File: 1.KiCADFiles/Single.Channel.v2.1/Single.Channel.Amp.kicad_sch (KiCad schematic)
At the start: 18 parts, among them J2 Conn_01x08, J3 Conn_01x04, J4 Conn_Coaxial_In, J5 Conn_Coaxial_Out, Q1 MMBT3904, Q2 MMBT3906

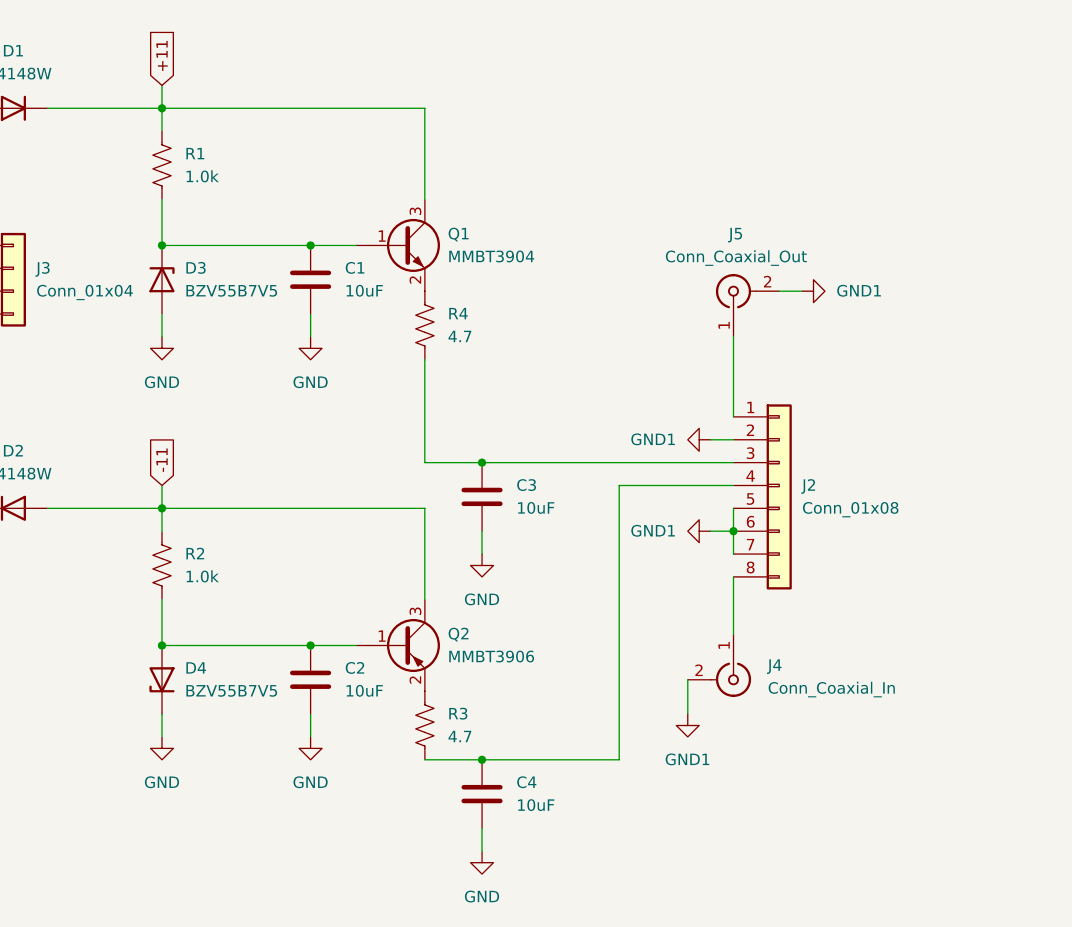
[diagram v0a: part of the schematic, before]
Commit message: Updated schematic with new Zener Component, updated componenet list
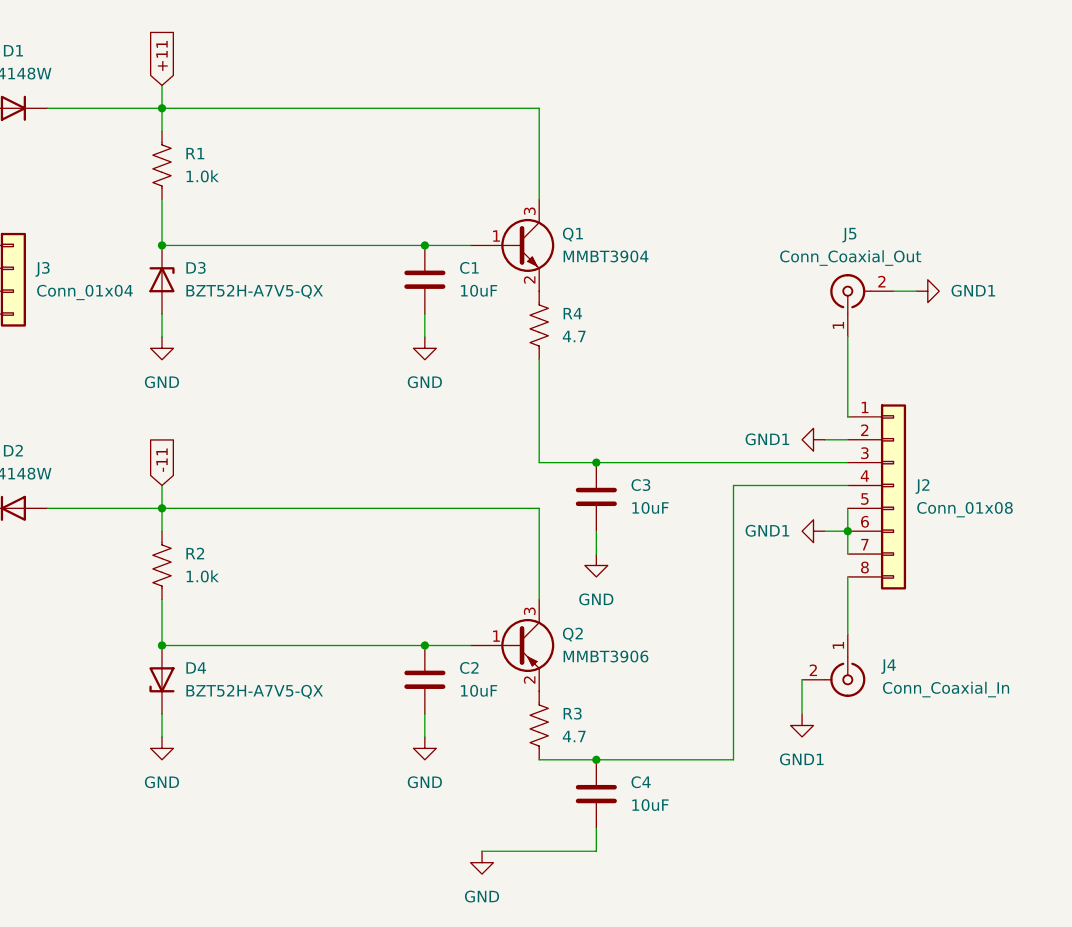
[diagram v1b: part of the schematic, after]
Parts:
- D3, D4: value BZV55B7V5 -> BZT52H-A7V5-QX
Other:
- moved on the sheet: C1, C2, C3, C4, J2, J4, J5, Q1, Q2, R3, R4

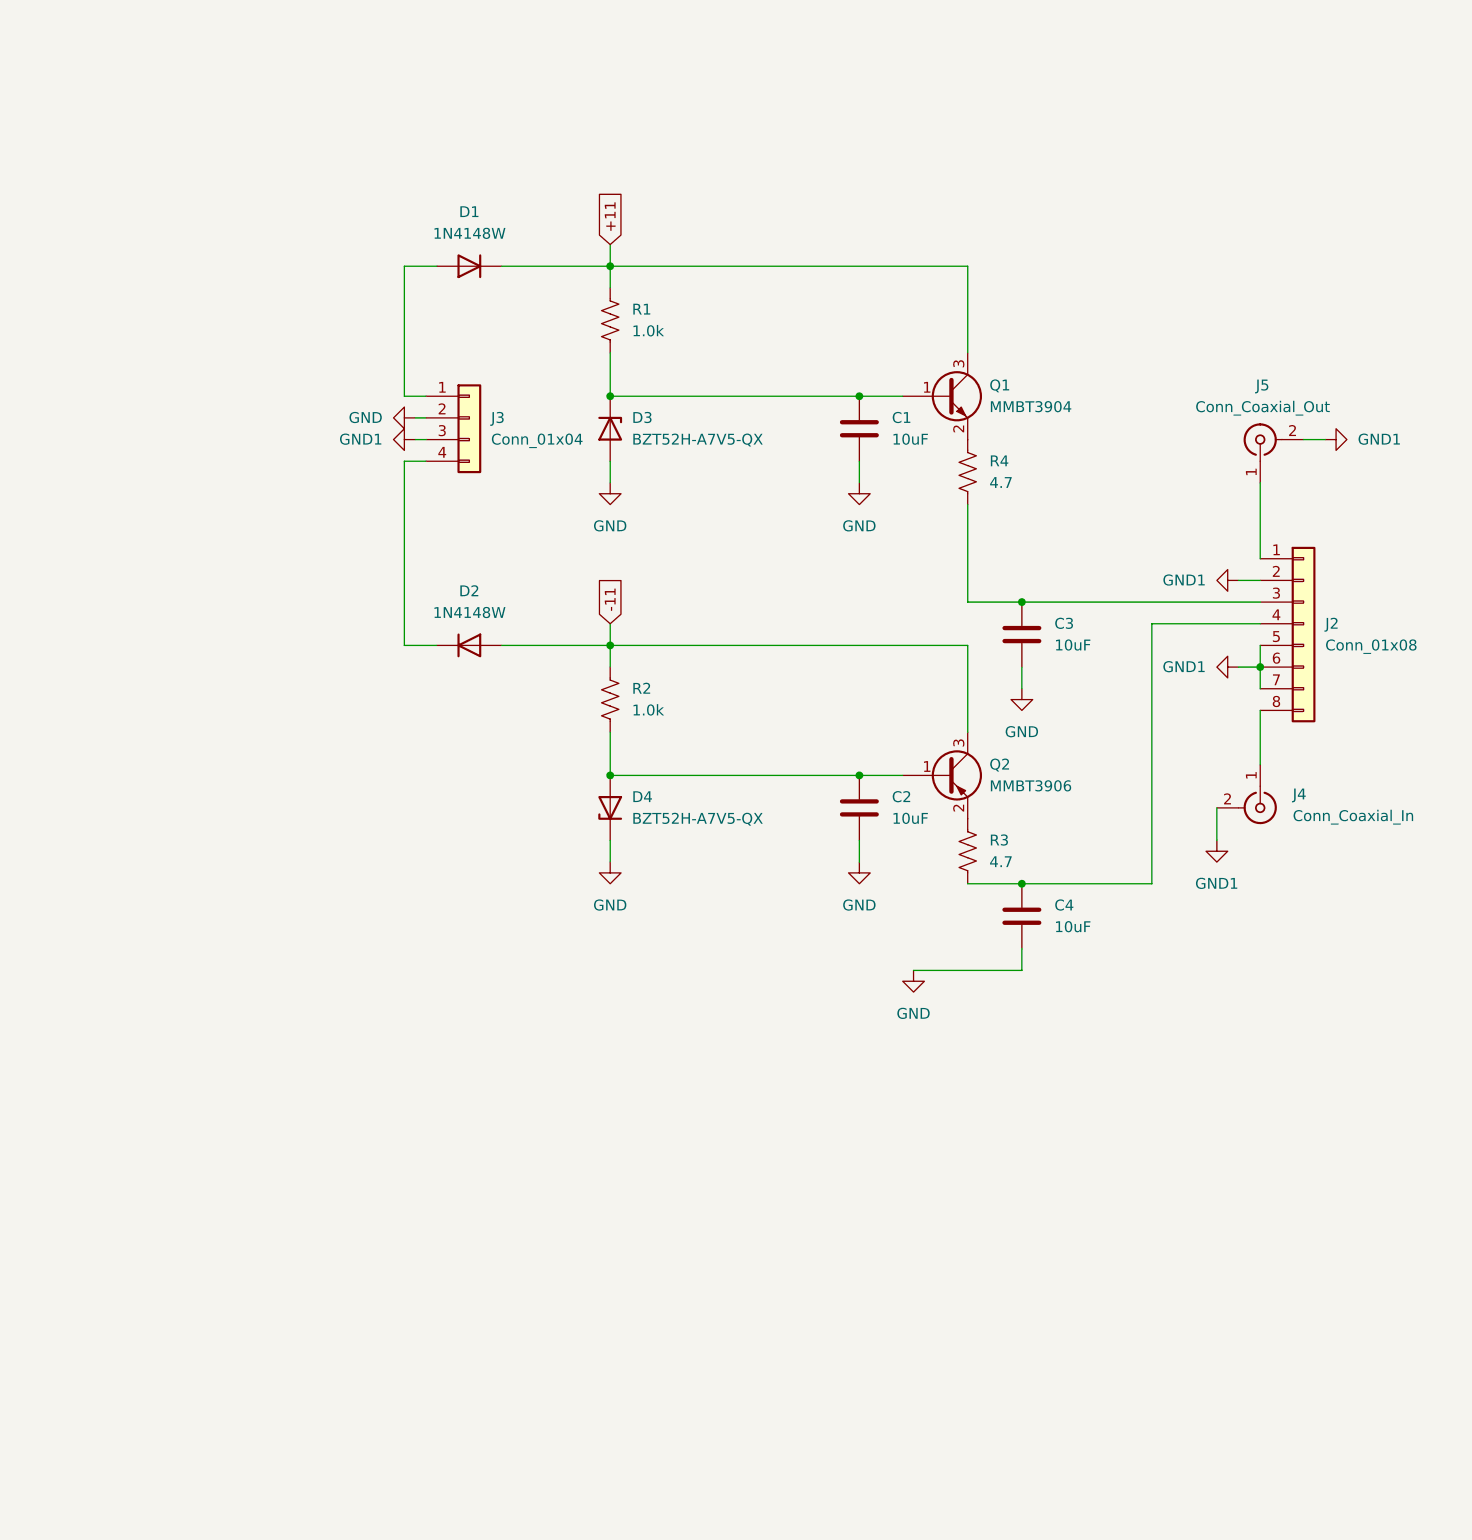
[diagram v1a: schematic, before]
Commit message: Updated Schematic Diagram for Single Channel Board
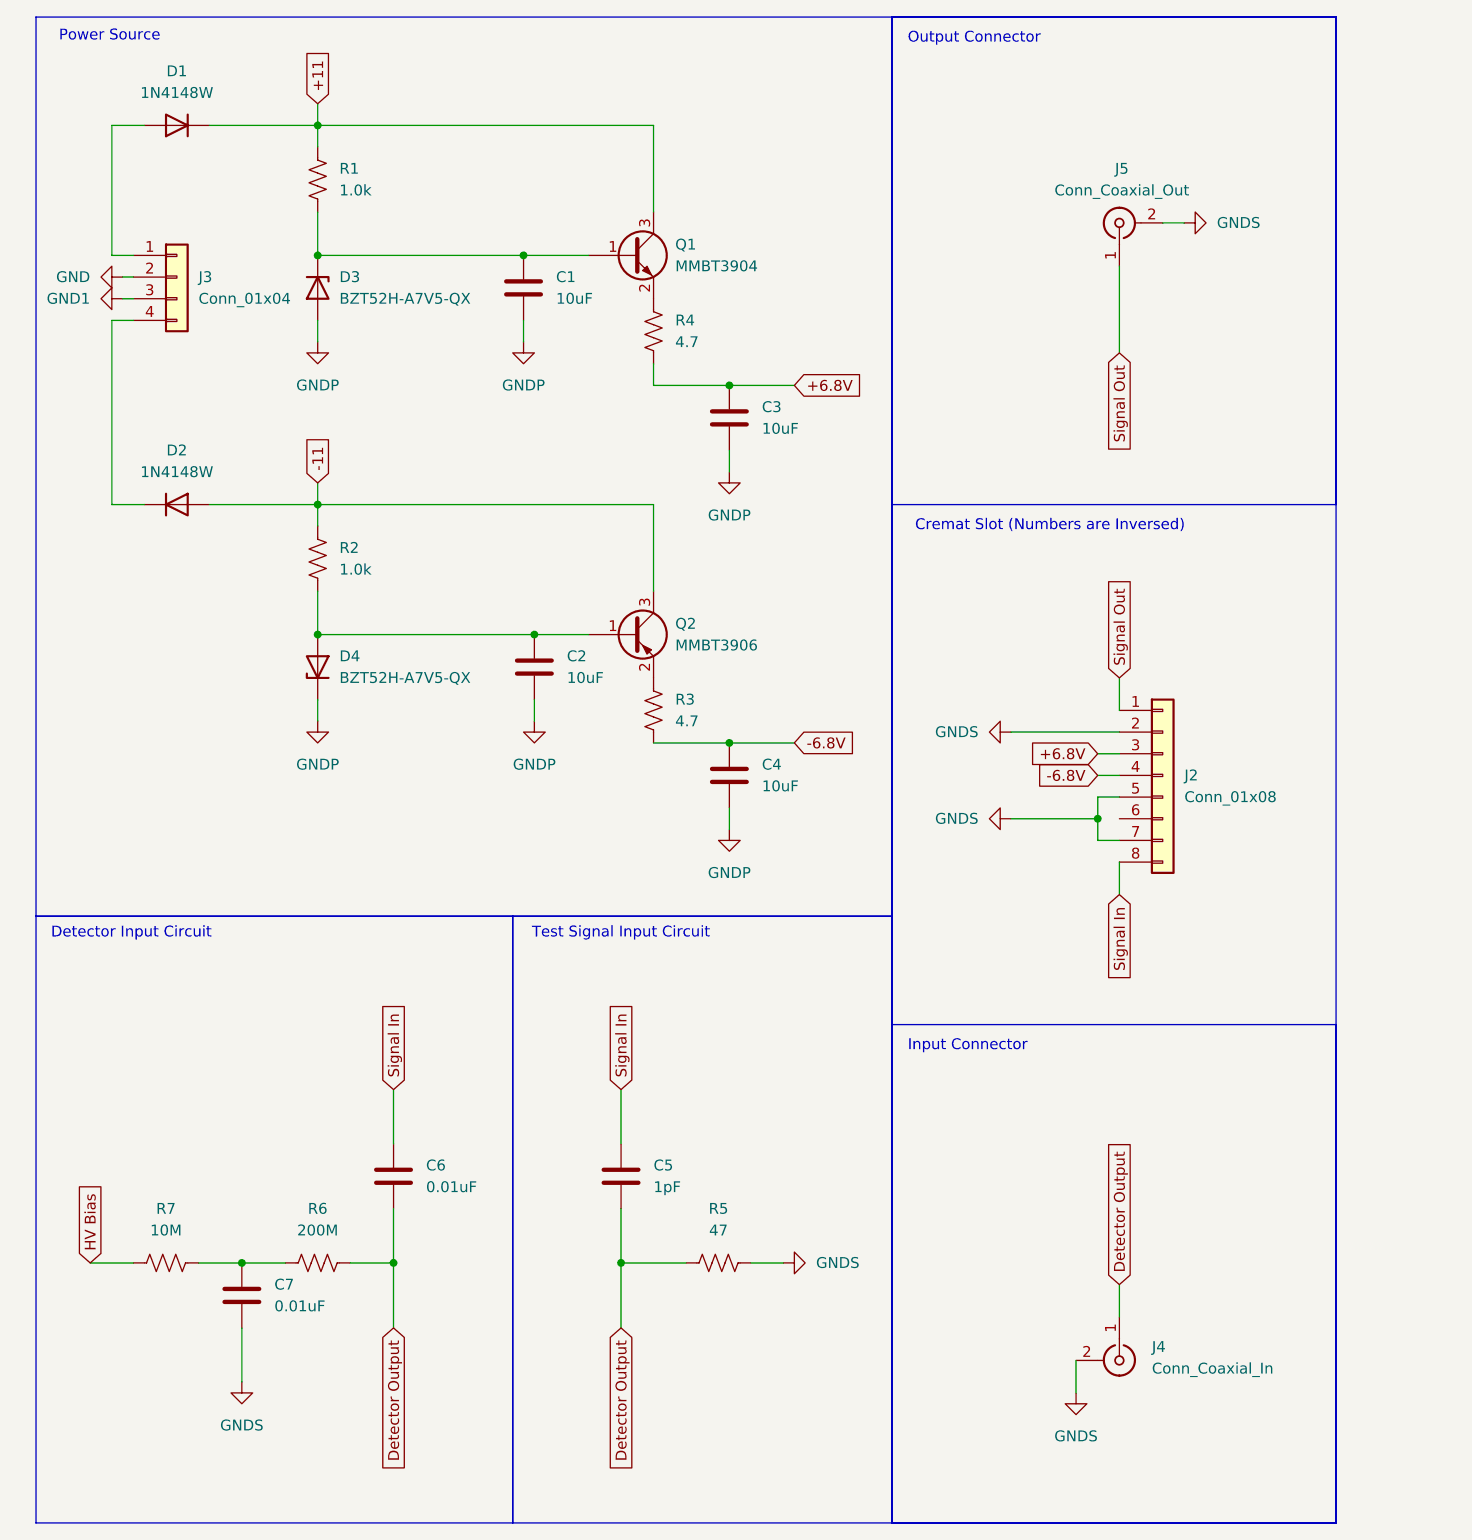
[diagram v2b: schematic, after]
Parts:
- added C5: 1pF, Capacitor_SMD:C_1206_3216Metric_Pad1.33x1.80mm_HandSolder, symbol Device:C
- added C6, C7: 0.01uF, Capacitor_SMD:C_1206_3216Metric_Pad1.33x1.80mm_HandSolder, symbol Device:C
- added R5: 47, Resistor_SMD:R_1206_3216Metric_Pad1.30x1.75mm_HandSolder, symbol Device:R_US
- added R6: 200M, Resistor_SMD:R_1206_3216Metric_Pad1.30x1.75mm_HandSolder, symbol Device:R_US
- added R7: 10M, Resistor_SMD:R_1206_3216Metric_Pad1.30x1.75mm_HandSolder, symbol Device:R_US
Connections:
- net GND: no longer C1.2, C2.2, C3.2, C4.2, D3.2 (A), D4.1 (K)
- net GND1: no longer J2.2 (GND), J2.5 (Pin_5), J2.6 (Pin_6), J2.7 (Pin_7), J4.2 (Ext), J5.2 (Ext)
- net Detector Output: now reaches J4.1 (In)
- net Detector Output: now also C5.2, C6.1, R5.2, R6.1; no longer J2.8 (Input)
- net -6.8V: now reaches C4.1, J2.4 (Pin_4), R3.2
- net Signal Out: now reaches J2.1 (Output), J5.1 (In)
- net +6.8V: now reaches C3.1, J2.3 (Pin_3), R4.2
- new net: C7.2, R6.2, R7.1
- new net GNDP: C1.2, C2.2, C3.2, C4.2, D3.2 (A), D4.1 (K)
- new net GNDS: C7.1, J2.2 (GND), J2.5 (Pin_5), J2.7 (Pin_7), J4.2 (Ext), J5.2 (Ext), R5.1
- new net HV Bias: R7.2
- new net Signal In: C5.1, C6.2, J2.8 (Input)
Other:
- note added: "Cremat Slot (Numbers are Inversed)"
- note added: "Detector Input Circuit"
- note added: "Input Connector"
- note added: "Output Connector"
- note added: "Power Source"
- note added: "Test Signal Input Circuit"
- moved on the sheet: C1, C2, C3, C4, D1, D2, D3, D4, J2, J3, J4, J5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
